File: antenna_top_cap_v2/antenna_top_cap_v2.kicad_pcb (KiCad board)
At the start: 4 copper layers, 100 x 100 mm, 69 parts, among them IC1 PCT2075DP,118, J1 Battery Charge Bypass, J10 USB_B_Micro, J11 USB_B_Micro, J13 USB_B_Micro, J14 BM04B-SRSS-TB(LF)(SN), J15 USB_B_Micro, J16 BM04B-SRSS-TB(LF)(SN), J17 BM04B-SRSS-TB(LF)(SN), J18 BM04B-SRSS-TB(LF)(SN)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

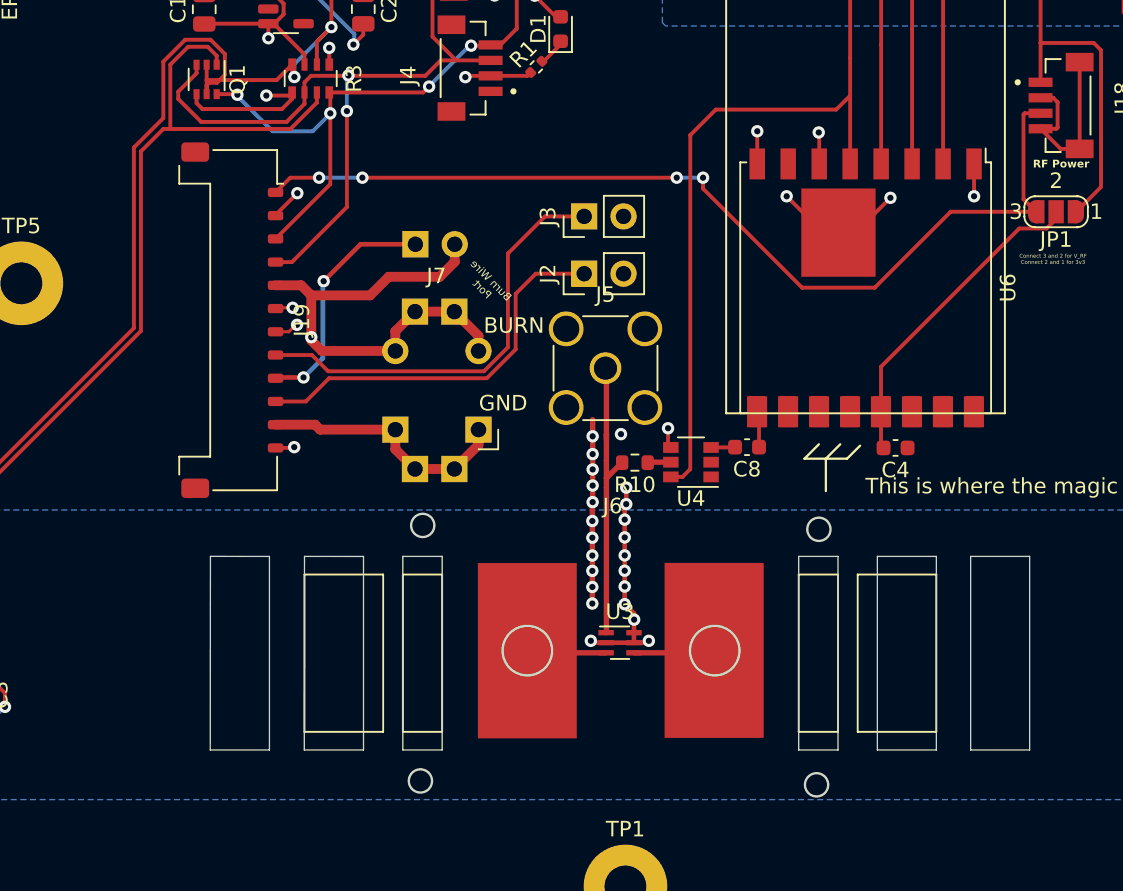
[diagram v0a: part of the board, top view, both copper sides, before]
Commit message: Swapped Balun
New Balun Part Number!
Minicircuits: NCS1.5-232+

Schematic and PCB Layout Updated
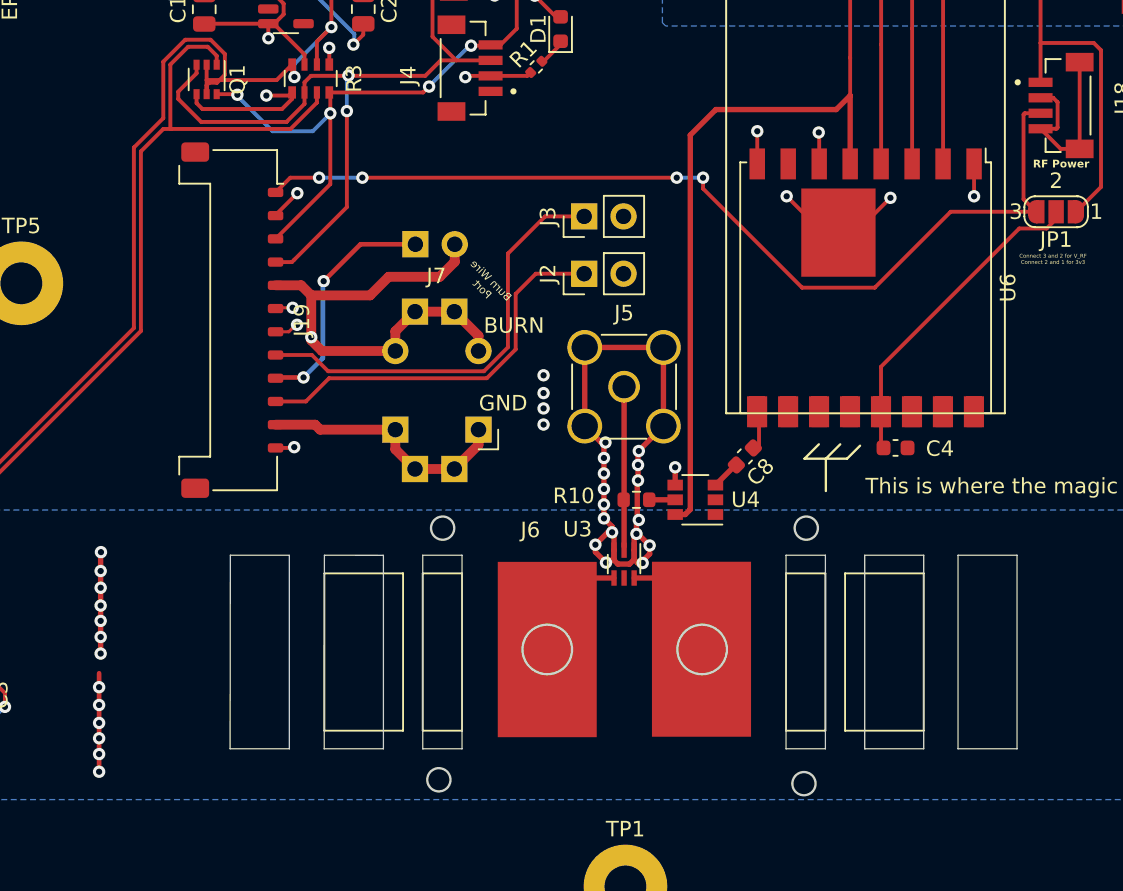
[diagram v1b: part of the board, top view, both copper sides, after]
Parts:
- removed REF**: Val**, mainboard:XYZ_cubesat-top
- J2: value Conn_01x02 -> EPS USB Bootselect Jumper
- J3: value Conn_01x02 -> EPS Reset Jumper
- moved U3 5.09 mm to (165.7, 130.4), turned to -90 degrees
- moved U4 2.45 mm to (170.3, 126.2)
- moved R10 2.40 mm to (166.5, 126.2)
- moved J5 1.70 mm to (165.7, 118.9)
- moved J6 0.79 mm to (165.8, 127.0)
- moved C8 0.62 mm to (173.5, 123.4), turned to -135 degrees
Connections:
- net 3.3V renamed +3V3
- IC1 pad 1: SDA1 -> SCL1
- J19 pad 4: SDA1 -> SCL1
- J4 pad 3: SDA1 -> SCL1
- J8 pad 3: SDA1 -> SCL1
- Q1 pad 3: SDA1 -> SCL1
- Q1 pad 4: /SDA_3V -> /SCL_3V
- R3 pad 5: /SDA_3V -> /SCL_3V
- R3 pad 6: SDA1 -> SCL1
- U1 pad 6: /SDA_3V -> /SCL_3V
- U3 pad 1: Net-(J5-In) -> GND
- U3 pad 2: GND -> Net-(J5-In)
- U3 pad 3: Net-(J6-tape_1) -> GND
- U3 pad 4: Net-(J6-tape_2) -> Net-(J6-tape_1)
- U3 pad 5: GND -> unconnected-(U3-NC-Pad5)
- U3 pad 6: GND -> Net-(J6-tape_2)
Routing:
- net SDA1: track 62.1 -> 0.00 mm, vias 2 -> 0
- net SCL1: track 52.0 -> 114.1 mm, vias 4 -> 6
- net /SDA_3V: track 58.3 -> 0.00 mm, vias 2 -> 0
- net /SCL_3V: track 69.3 -> 127.6 mm, vias 1 -> 3
- net GND: track 201.1 -> 230.4 mm, vias 39 -> 49
- net Net-(J5-In): track 18.1 -> 10.3 mm
- net Net-(J6-tape_1): track 6.97 -> 1.66 mm
- net Net-(J6-tape_2): track 6.06 -> 1.40 mm
- net SPI0_CS0: track 60.8 -> 63.1 mm
- net Net-(U4-input2): track 1.55 -> 2.07 mm

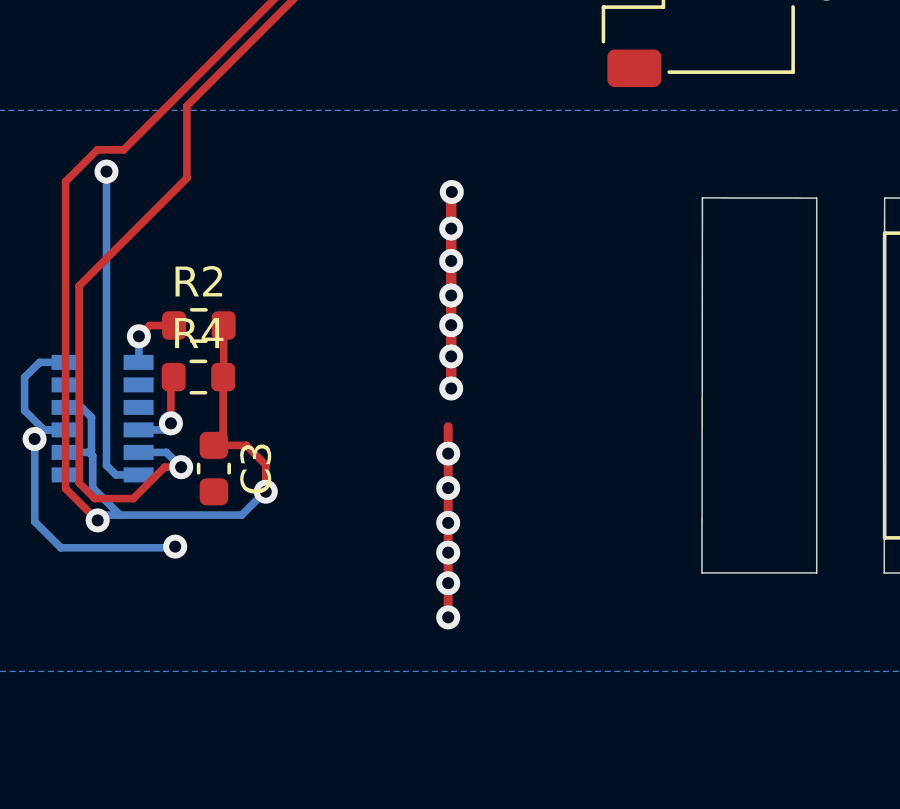
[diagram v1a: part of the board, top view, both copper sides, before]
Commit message: Added Schematic Symbols for FC Debug Port
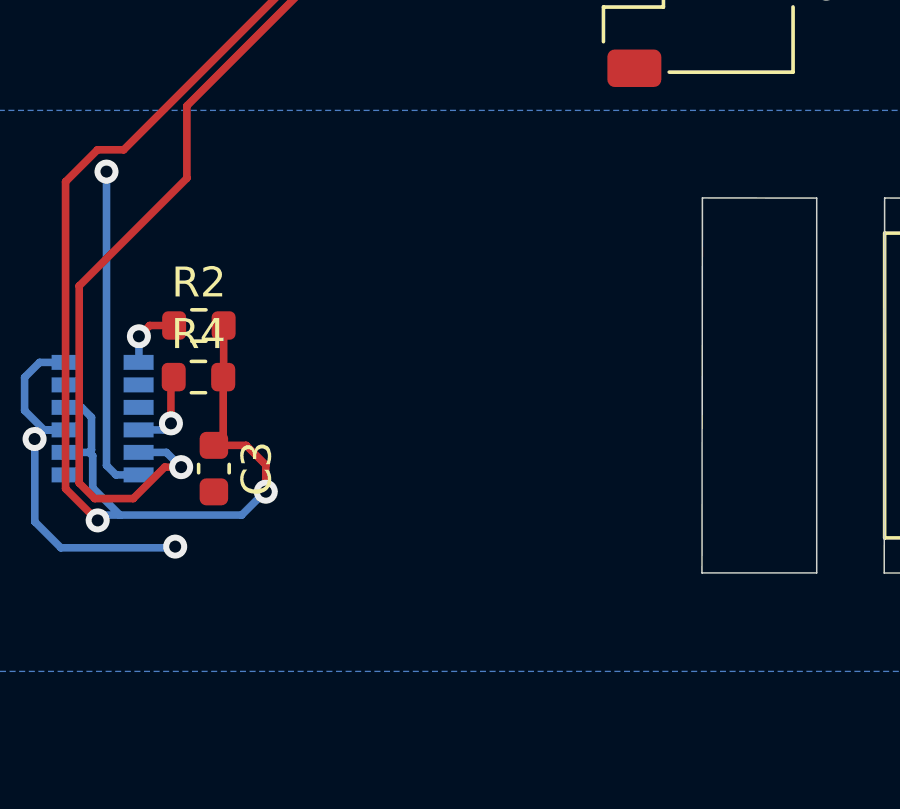
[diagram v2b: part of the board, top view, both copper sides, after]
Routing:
- net GND: track 230.4 -> 217.5 mm, vias 49 -> 36
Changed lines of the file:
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@@
-	)
-	(segment
-		(start 131.9458 129.6194)
-		(end 131.9658 129.5994)
-		(width 0.34925)
-		(layer "F.Cu")
-		(net 1)
-	)
-	(segment
-		(start 131.8458 143.7794)
-		(end 131.8458 138.3194)
-		(width 0.3)
-		(layer "F.Cu")
-		(net 1)
 	)
 	(segment
@@
 	)
 	(segment
-		(start 131.9458 130.8194)
-		(end 131.9458 136.1494)
-		(width 0.34925)
-		(layer "F.Cu")
-		(net 1)
-	)
-	(segment
 		(start 148.9058 95.4844)
 		(end 148.9058 96.1844)
@@
 		(end 123.2658 82.8894)
 		(width 0.25)
-		(layer "F.Cu")
-		(net 1)
-	)
-	(segment
-		(start 131.9458 130.8194)
-		(end 131.9458 129.6194)
-		(width 0.34925)
 		(layer "F.Cu")
 		(net 1)
@@
 	)
 	(segment
-		(start 131.8458 138.3194)
-		(end 131.8458 137.4194)
-		(width 0.3)
-		(layer "F.Cu")
-		(net 1)
-	)
-	(segment
 		(start 163.8958 129.1194)
 		(end 163.8958 129.593414)
@@
 	)
 	(via
-		(at 131.9458 133.0494)
+		(at 122.5358 83.6194)
+		(size 0.8)
+		(drill 0.4)
+		(layers "F.Cu" "B.Cu")
+		(net 1)
+	)
+	(via
+		(at 188.3458 106.6194)
+		(size 0.8)
+		(drill 0.4)
+		(layers "F.Cu" "B.Cu")
+		(net 1)
+	)
+	(via
+		(at 182.9458 106.7194)
+		(size 0.8)
+		(drill 0.4)
+		(layers "F.Cu" "B.Cu")
+		(net 1)
+	)
+	(via
+		(at 166.6958 123.0694)
+		(size 0.8)
+		(drill 0.4)
+		(layers "F.Cu" "B.Cu")
+		(net 1)
+	)
+	(via
+		(at 176.2458 106.6194)
+		(size 0.8)
+		(drill 0.4)
+		(layers "F.Cu" "B.Cu")
+		(net 1)
+	)
+	(via
+		(at 144.4458 122.8194)
+		(size 0.8)
+		(drill 0.4)
+		(layers "F.Cu" "B.Cu")
+		(net 1)
+	)
+	(via
+		(at 122.7458 141.4194)
+		(size 0.8)
+		(drill 0.4)
+		(layers "F.Cu" "B.Cu")
+		(net 1)
+	)
+	(via
+		(at 209.0758 78.9794)
+		(size 0.8)
+		(drill 0.4)
+		(layers "F.Cu" "B.Cu")
+		(net 1)
+	)
+	(via
+		(at 160.5458 119.3294)
 		(size 0.8)
 		(drill 0.4)
@@
 	)
 	(via
-		(at 131.8458 138.3194)
+		(at 164.4458 125.5194)
+		(size 0.8)
+		(drill 0.4)
+		(layers "F.Cu" "B.Cu")
+		(net 1)
+	)
+	(via
+		(at 159.9758 93.6644)
+		(size 0.8)
+		(drill 0.4)
+		(layers "F.Cu" "B.Cu")
+		(net 1)
+	)
+	(via
+		(at 166.6458 124.9694)
+		(size 0.8)
+		(drill 0.4)
+		(layers "F.Cu" "B.Cu")
+		(net 1)
+	)
+	(via
+		(at 145.5458 115.7194)
+		(size 0.8)
+		(drill 0.4)
+		(layers "F.Cu" "B.Cu")
+		(net 1)
+	)
+	(via
+		(at 160.5458 120.3194)
 		(size 0.8)
 		(drill 0.4)
@@
 	)
 	(via
-		(at 122.5358 83.6194)
-		(size 0.8)
-		(drill 0.4)
-		(layers "F.Cu" "B.Cu")
-		(net 1)
-	)
-	(via
-		(at 188.3458 106.6194)
-		(size 0.8)
-		(drill 0.4)
-		(layers "F.Cu" "B.Cu")
-		(net 1)
-	)
-	(via
-		(at 182.9458 106.7194)
-		(size 0.8)
-		(drill 0.4)
-		(layers "F.Cu" "B.Cu")
-		(net 1)
-	)
-	(via
-		(at 131.9458 134.0394)
+		(at 167.3958 129.1694)
+		(size 0.8)
+		(drill 0.4)
+		(layers "F.Cu" "B.Cu")
+		(net 1)
+	)
+	(via
+		(at 164.4458 123.5194)
+		(size 0.8)
+		(drill 0.4)
+		(layers "F.Cu" "B.Cu")
+		(net 1)
+	)
+	(via
+		(at 118.058855 137.832994)
+		(size 0.8)
+		(drill 0.4)
+		(layers "F.Cu" "B.Cu")
+		(net 1)
+	)
+	(via
+		(at 160.5458 121.3594)
 		(size 0.8)
 		(drill 0.4)
@@
 	)
 	(via
-		(at 166.6958 123.0694)
-		(size 0.8)
-		(drill 0.4)
-		(layers "F.Cu" "B.Cu")
-		(net 1)
-	)
-	(via
-		(at 131.9458 135.0794)
-		(size 0.8)
-		(drill 0.4)
-		(layers "F.Cu" "B.Cu")
-		(free yes)
-		(net 1)
-	)
-	(via
-		(at 176.2458 106.6194)
-		(size 0.8)
-		(drill 0.4)
-		(layers "F.Cu" "B.Cu")
-		(net 1)
-	)
-	(via
-		(at 144.4458 122.8194)
-		(size 0.8)
-		(drill 0.4)
-		(layers "F.Cu" "B.Cu")
-		(net 1)
-	)
-	(via
-		(at 131.9458 130.8194)
-		(size 0.8)
-		(drill 0.4)
-		(layers "F.Cu" "B.Cu")
-		(free yes)
-		(net 1)
-	)
-	(via
-		(at 131.8458 140.6294)
-		(size 0.8)
-		(drill 0.4)
-		(layers "F.Cu" "B.Cu")
-		(free yes)
-		(net 1)
-	)
-	(via
-		(at 131.8458 141.6194)
-		(size 0.8)
-		(drill 0.4)
-		(layers "F.Cu" "B.Cu")
-		(free yes)
-		(net 1)
-	)
-	(via
-		(at 122.7458 141.4194)
-		(size 0.8)
-		(drill 0.4)
-		(layers "F.Cu" "B.Cu")
-		(net 1)
-	)
-	(via
-		(at 209.0758 78.9794)
-		(size 0.8)
-		(drill 0.4)
-		(layers "F.Cu" "B.Cu")
-		(net 1)
-	)
-	(via
-		(at 160.5458 119.3294)
-		(size 0.8)
-		(drill 0.4)
-		(layers "F.Cu" "B.Cu")
-		(free yes)
-		(net 1)
-	)
-	(via
-		(at 131.8458 142.6394)
-		(size 0.8)
-		(drill 0.4)
-		(layers "F.Cu" "B.Cu")
-		(free yes)
-		(net 1)
-	)
-	(via
-		(at 164.4458 125.5194)
-		(size 0.8)
-		(drill 0.4)
-		(layers "F.Cu" "B.Cu")
-		(net 1)
-	)
-	(via
-		(at 131.8458 143.7794)
-		(size 0.8)
-		(drill 0.4)
-		(layers "F.Cu" "B.Cu")
-		(free yes)
-		(net 1)
-	)
-	(via
-		(at 159.9758 93.6644)
-		(size 0.8)
-		(drill 0.4)
-		(layers "F.Cu" "B.Cu")
-		(net 1)
-	)
-	(via
-		(at 166.6458 124.9694)
-		(size 0.8)
-		(drill 0.4)
-		(layers "F.Cu" "B.Cu")
-		(net 1)
-	)
-	(via
-		(at 145.5458 115.7194)
-		(size 0.8)
-		(drill 0.4)
-		(layers "F.Cu" "B.Cu")
-		(net 1)
-	)
-	(via
-		(at 160.5458 120.3194)
-		(size 0.8)
-		(drill 0.4)
-		(layers "F.Cu" "B.Cu")
-		(free yes)
-		(net 1)
-	)
-	(via
-		(at 167.3958 129.1694)
-		(size 0.8)
-		(drill 0.4)
-		(layers "F.Cu" "B.Cu")
-		(net 1)
-	)
-	(via
-		(at 164.4458 123.5194)
-		(size 0.8)
-		(drill 0.4)
-		(layers "F.Cu" "B.Cu")
-		(net 1)
-	)
-	(via
-		(at 118.058855 137.832994)
-		(size 0.8)
-		(drill 0.4)
-		(layers "F.Cu" "B.Cu")
-		(net 1)
-	)
-	(via
-		(at 160.5458 121.3594)
-		(size 0.8)
-		(drill 0.4)
-		(layers "F.Cu" "B.Cu")
-		(free yes)
-		(net 1)
-	)
-	(via
 		(at 166.6958 127.5194)
 		(size 0.8)
@@
 	)
 	(via
-		(at 131.9658 129.5994)
-		(size 0.8)
-		(drill 0.4)
-		(layers "F.Cu" "B.Cu")
-		(free yes)
-		(net 1)
-	)
-	(via
 		(at 163.8958 129.1194)
 		(size 0.8)
@@
 	)
 	(via
-		(at 131.8458 139.4694)
-		(size 0.8)
-		(drill 0.4)
-		(layers "F.Cu" "B.Cu")
-		(free yes)
-		(net 1)
-	)
-	(via
 		(at 164.4458 126.5194)
 		(size 0.8)
@@
 	)
 	(via
-		(at 131.9458 136.1494)
-		(size 0.8)
-		(drill 0.4)
-		(layers "F.Cu" "B.Cu")
-		(free yes)
-		(net 1)
-	)
-	(via
 		(at 160.5458 118.1794)
 		(size 0.8)
 		(drill 0.4)
-		(layers "F.Cu" "B.Cu")
-		(free yes)
-		(net 1)
-	)
-	(via
-		(at 131.9458 131.8994)
-		(size 0.8)
-		(drill 0.4)

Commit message: SDA / SCL Hotfix
See this issue: https://github.com/proveskit/antenna-board/issues/6
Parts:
- added J12: FC Board Connector, FC_DEV_BOARD:MOLEX_5040500591, F.Cu at (104.3, 107.9)
- added J20: FC USB Bootselect Jumper, Connector_PinHeader_2.54mm:PinHeader_1x02_P2.54mm_Vertical, F.Cu at (105.2, 92.9)
- J10: value USB_B_Micro -> USB_B_Micro_FC
- J11: value USB_B_Micro -> USB_B_Micro_EPS
- J19: value Z+_Cap_Connector -> EPS Board Connector
- J9: value BM04B-SRSS-TB(LF)(SN) -> FC Reset Jumper; footprint Antenna_board:JST_BM04B-SRSS-TB(LF)(SN) -> Connector_PinHeader_2.54mm:PinHeader_1x02_P2.54mm_Vertical
- U3: value 0433BM15A0001 -> NCS1.5-232+
- moved J9 31.0 mm to (105.2, 96.7)
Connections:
- net USBBOOT renamed EPS_USBBOOT
- net USB_D+ renamed EPS_USB_D+
- net USB_D- renamed EPS_USB_D-
- net ~{RESET} renamed ~{EPS_RESET}
- IC1 pad 1: SCL1 -> SDA1
- J10 pad 2: /1d- -> FC_USB_D-
- J10 pad 3: /1d+ -> FC_USB_D+
- J19 pad 4: SCL1 -> SDA1
- J4 pad 3: SCL1 -> SDA1
- J8 pad 3: SCL1 -> SDA1
- J9 pad 1: Net-(J10-VBUS) -> ~{FC_RESET}
- J9 pad 2: /1d- -> GND
- Q1 pad 3: SCL1 -> SDA1
- Q1 pad 4: /SCL_3V -> SDA_3V
- R3 pad 5: /SCL_3V -> SDA_3V
- R3 pad 6: SCL1 -> SDA1
- U1 pad 6: /SCL_3V -> SDA_3V
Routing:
- net SDA1: track 0.00 -> 62.1 mm, vias 0 -> 2
- net SCL1: track 114.1 -> 52.0 mm, vias 6 -> 4
- net SDA_3V: track 0.00 -> 58.3 mm, vias 0 -> 2
- net /SCL_3V: track 127.6 -> 69.3 mm, vias 3 -> 1
- net FC_USB_D+: track 0.00 -> 10.8 mm, vias 0 -> 1
- net /1d+: track 10.8 -> 0.00 mm, vias 1 -> 0
- net FC_USB_D-: track 0.00 -> 10.3 mm, vias 0 -> 1
- net /1d-: track 10.3 -> 0.00 mm, vias 1 -> 0
